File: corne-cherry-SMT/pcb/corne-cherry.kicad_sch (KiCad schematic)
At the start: 140 parts, among them J1 MJ-4PP-9, J2 OLED, J3 MJ-4PP-9, J4 OLED, J5 Conn_01x02, J6 Conn_01x02, J7 Conn_01x05_MountingPin, J8 Conn_01x05_MountingPin, SW1 SW_PUSH, SW10 SW_PUSH, SW11 SW_PUSH, SW12 SW_PUSH, SW13 SW_PUSH, SW14 SW_PUSH, SW15 SW_PUSH, SW16 SW_PUSH, SW17 SW_PUSH, SW18 SW_PUSH, SW19 SW_PUSH, SW2 SW_PUSH, SW20 SW_PUSH, SW21 SW_PUSH, SW22 SW_PUSH, SW23 SW_PUSH, SW24 SW_PUSH, SW25 SW_PUSH, SW26 SW_PUSH, SW27 SW_PUSH, SW28 SW_PUSH, SW29 SW_PUSH, SW3 SW_PUSH, SW30 SW_PUSH, SW31 SW_PUSH, SW32 SW_PUSH, SW33 SW_PUSH, SW34 SW_PUSH, SW35 SW_PUSH, SW36 SW_PUSH, SW37 SW_PUSH, SW38 SW_PUSH, SW39 SW_PUSH, SW4 SW_PUSH, SW40 SW_PUSH, SW41 SW_PUSH, SW42 SW_PUSH, SW43 SW_PUSH, SW44 SW_PUSH, SW5 SW_PUSH, SW6 SW_PUSH, SW7 SW_PUSH, SW8 SW_PUSH, SW9 SW_PUSH, U2 ProMicro, U3 ProMicro_r

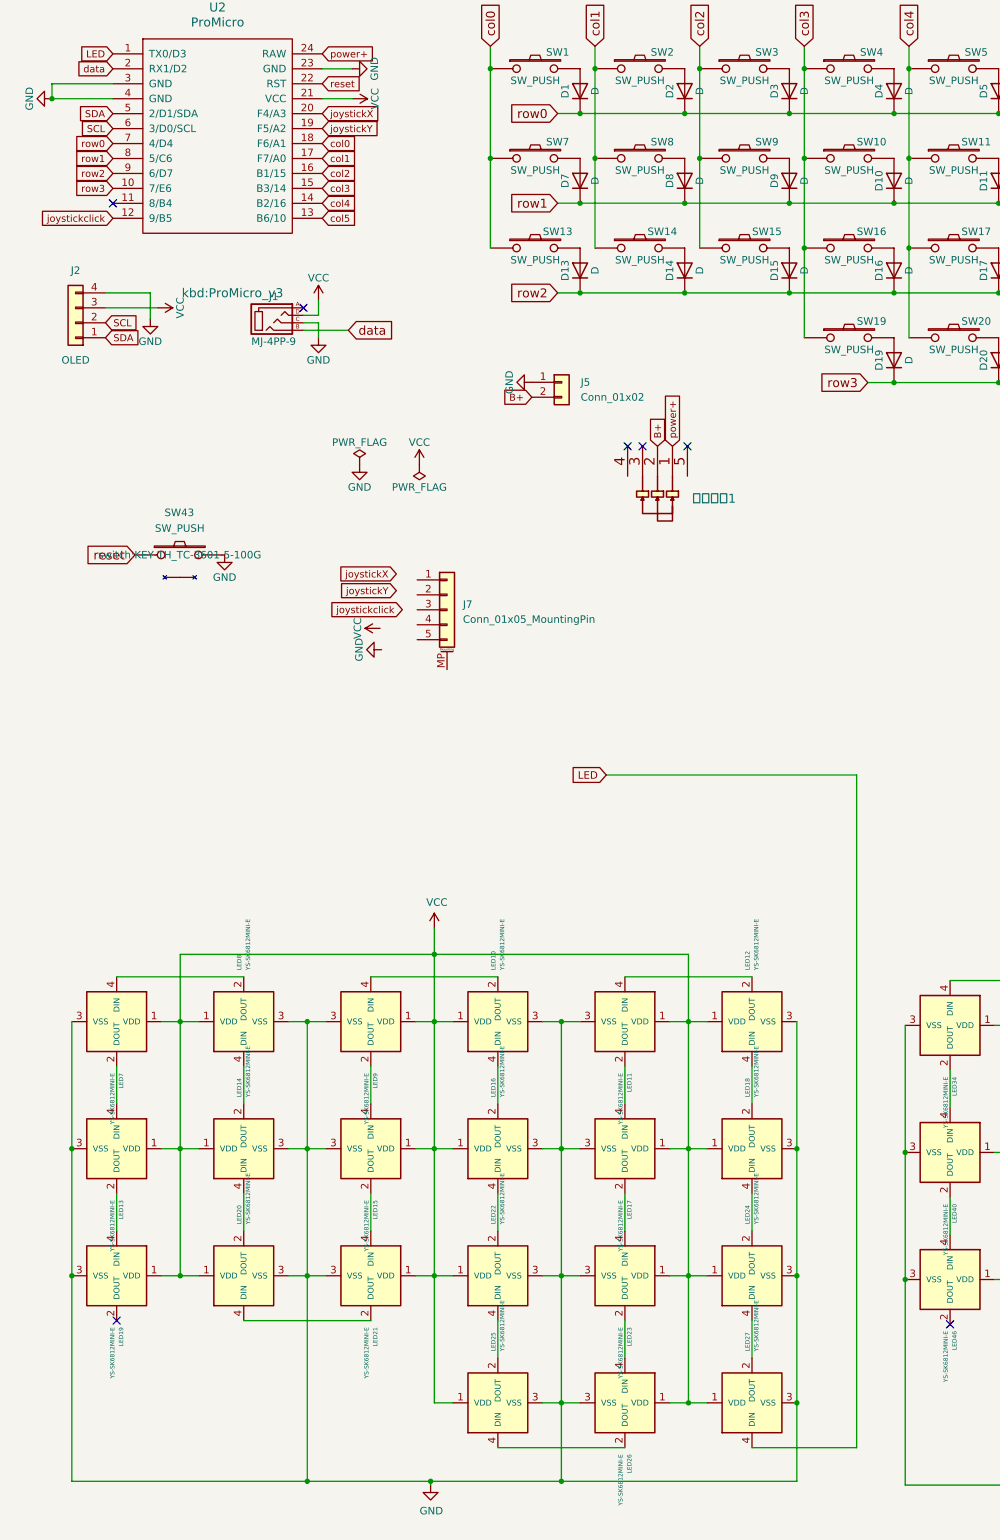
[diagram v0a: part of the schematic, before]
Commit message: add rotate encoder in the left
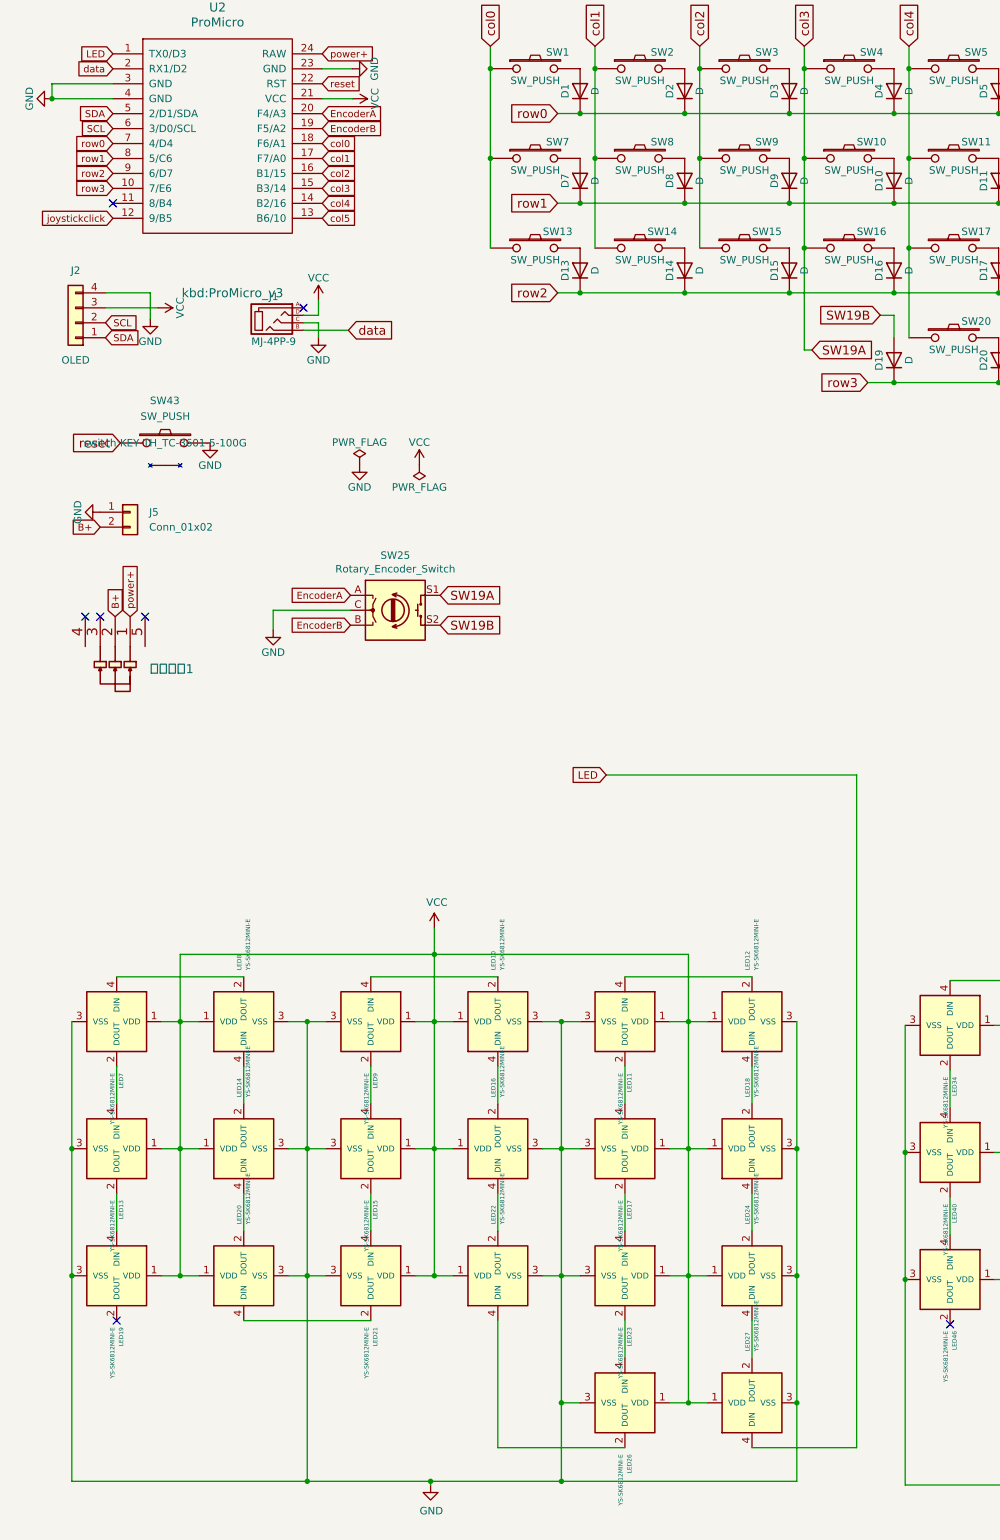
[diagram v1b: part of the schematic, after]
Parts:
- removed J7: Conn_01x05_MountingPin, Connector_FFC-FPC:Molex_200528-0050_1x05-1MP_P1.00mm_Horizontal, symbol Connector_Generic_MountingPin:Conn_01x05_MountingPin
- removed LED25: YS-SK6812MINI-E, kbd:YS-SK6812MINI-E, symbol kbd:YS-SK6812MINI-E
- removed SW19: SW_PUSH, kbd:CherryMX_Hotswap, symbol kbd:SW_PUSH
- added SW25: Rotary_Encoder_Switch, SofleKeyboard-footprint:RotaryEncoder_Alps_EC11E-Switch_Vertical_H20mm-keebio_modified, symbol SofleKeyboard-rescue:Rotary_Encoder_Switch-Device
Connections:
- net GND: now also SW25.C
- net SW19B: now reaches D19.2 (A)
- net SW19B: now also SW25.S2
- net at LED22.4 (DIN): now also LED26.2 (DOUT)
- net col3 renamed SW19A
- net SW19A: now also SW25.S1
- net joystickX renamed EncoderA
- net EncoderA: now also SW25.A
- net joystickY renamed EncoderB
- net EncoderB: now also SW25.B
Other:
- moved on the sheet: J5, SW43, 卧式开关1
